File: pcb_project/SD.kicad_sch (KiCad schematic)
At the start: 0 parts

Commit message: Create MicroSD circuit
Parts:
- added C1: 0.1 µF, symbol Device:C
- added C2: 10µF, symbol Device:C
- added J1: MEM2052-00-195-00-A, Project_Footprints:MEM20520019500A, symbol MEM2052-00-195-00-A:MEM2052-00-195-00-A
- added R1, R2, R3, R4, R5, R6: 10k, symbol Device:R
- added R10, R11, R12, R7, R8, R9: R, symbol Device:R
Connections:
- new net: J1.7 (DAT0), R1.2, R7.2
- new net: J1.2 (CD/DAT3), R10.2, R4.2
- new net: J1.8 (DAT1), R2.2, R8.2
- new net: J1.3 (CMD), R11.2, R5.2
- new net: J1.1 (DAT2), R3.2, R9.2
- new net: J1.5 (CLK), R12.2
- new net +3V3: C1.1, C2.1, J1.4 (VDD), R1.1, R2.1, R3.1, R4.1, R5.1, R6.1
- new net GND: C1.2, C2.2, J1.6 (VSS), J1.G1 (GND_1), J1.G2 (GND_2), J1.G3 (GND_3), J1.G4 (GND_4)
- new net SDMMC_CLK: R12.1
- new net SDMMC_CMD: R11.1
- new net SDMMC_DAT0: R7.1
- new net SDMMC_DAT1: R8.1
- new net SDMMC_DAT2: R9.1
- new net SDMMC_DAT3: R10.1
- new net SD_CD: J1.9 (CD_PIN), R6.2
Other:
- note added: "R7-R12 should be physically close to MCU"

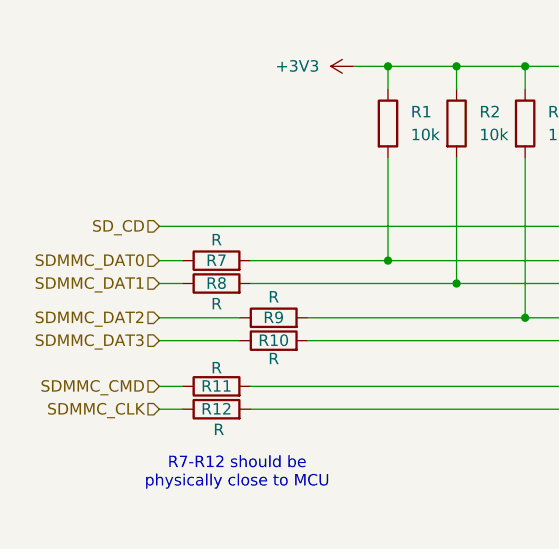
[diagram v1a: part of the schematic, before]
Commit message: Create power supply circuit
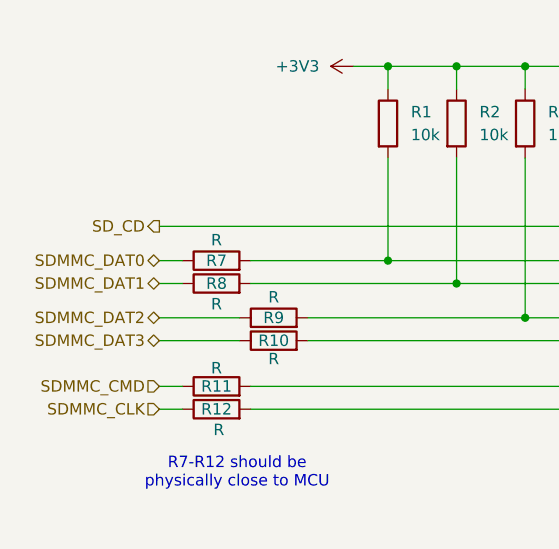
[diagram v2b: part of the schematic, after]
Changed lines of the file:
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@@
 	)
 	(hierarchical_label "SDMMC_DAT2"
-		(shape input)
+		(shape bidirectional)
 		(at 109.22 85.09 180)
 		(effects
@@
 	)
 	(hierarchical_label "SDMMC_DAT0"
-		(shape input)
+		(shape bidirectional)
 		(at 109.22 78.74 180)
 		(effects
@@
 	)
 	(hierarchical_label "SD_CD"
-		(shape input)
+		(shape output)
 		(at 109.22 74.93 180)
 		(effects
@@
 	)
 	(hierarchical_label "SDMMC_DAT3"
-		(shape input)
+		(shape bidirectional)
 		(at 109.22 87.63 180)
 		(effects
@@
 	)
 	(hierarchical_label "SDMMC_DAT1"
-		(shape input)
+		(shape bidirectional)
 		(at 109.22 81.28 180)
 		(effects

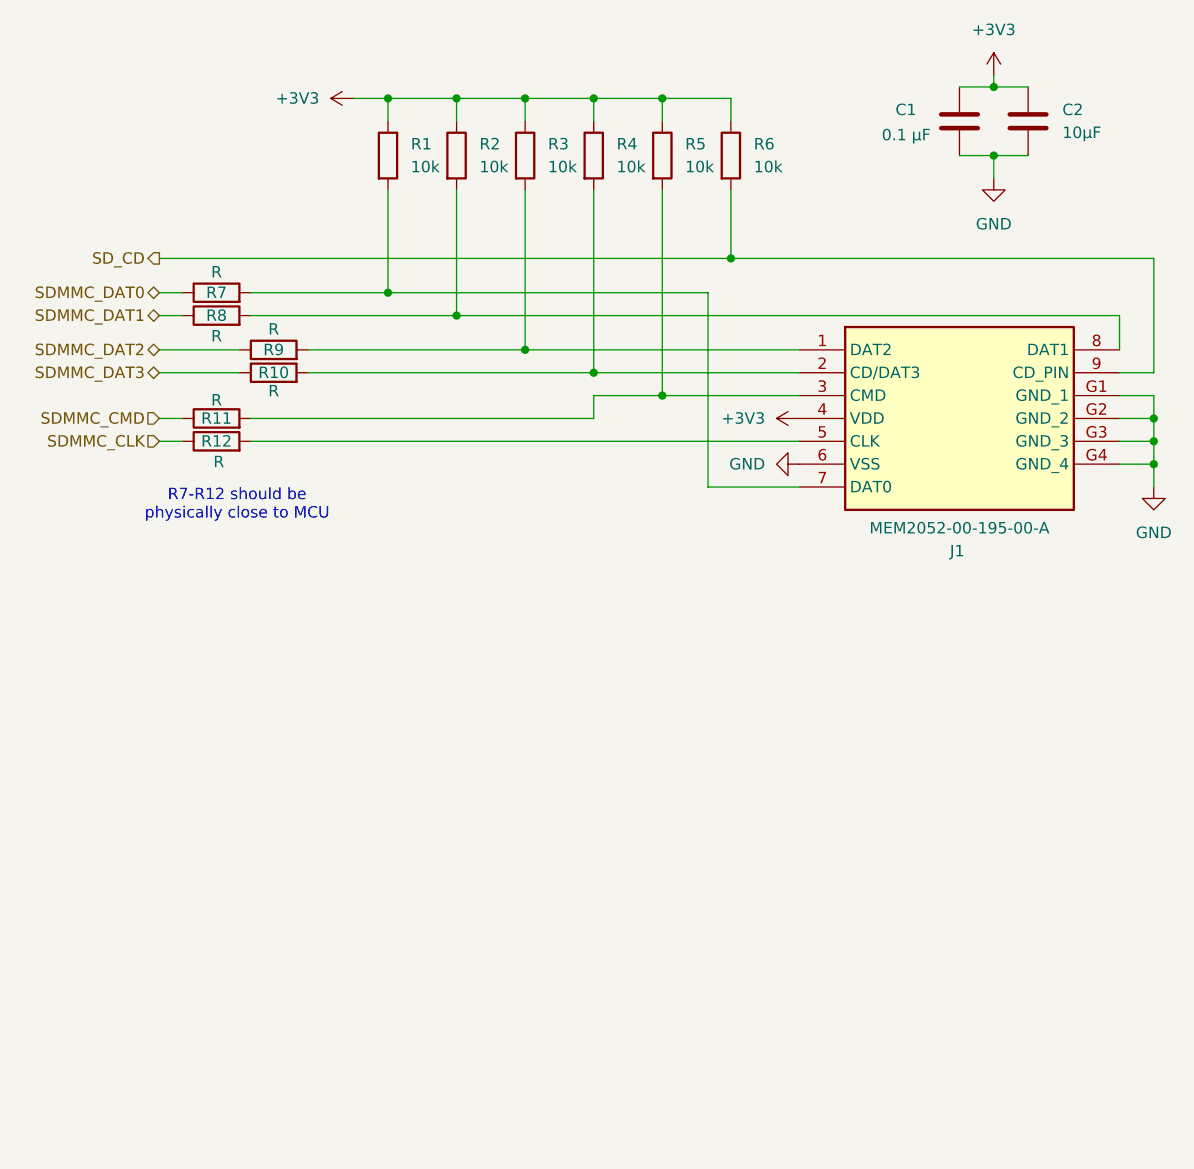
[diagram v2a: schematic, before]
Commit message: Add ESB protection to MicroSd reader
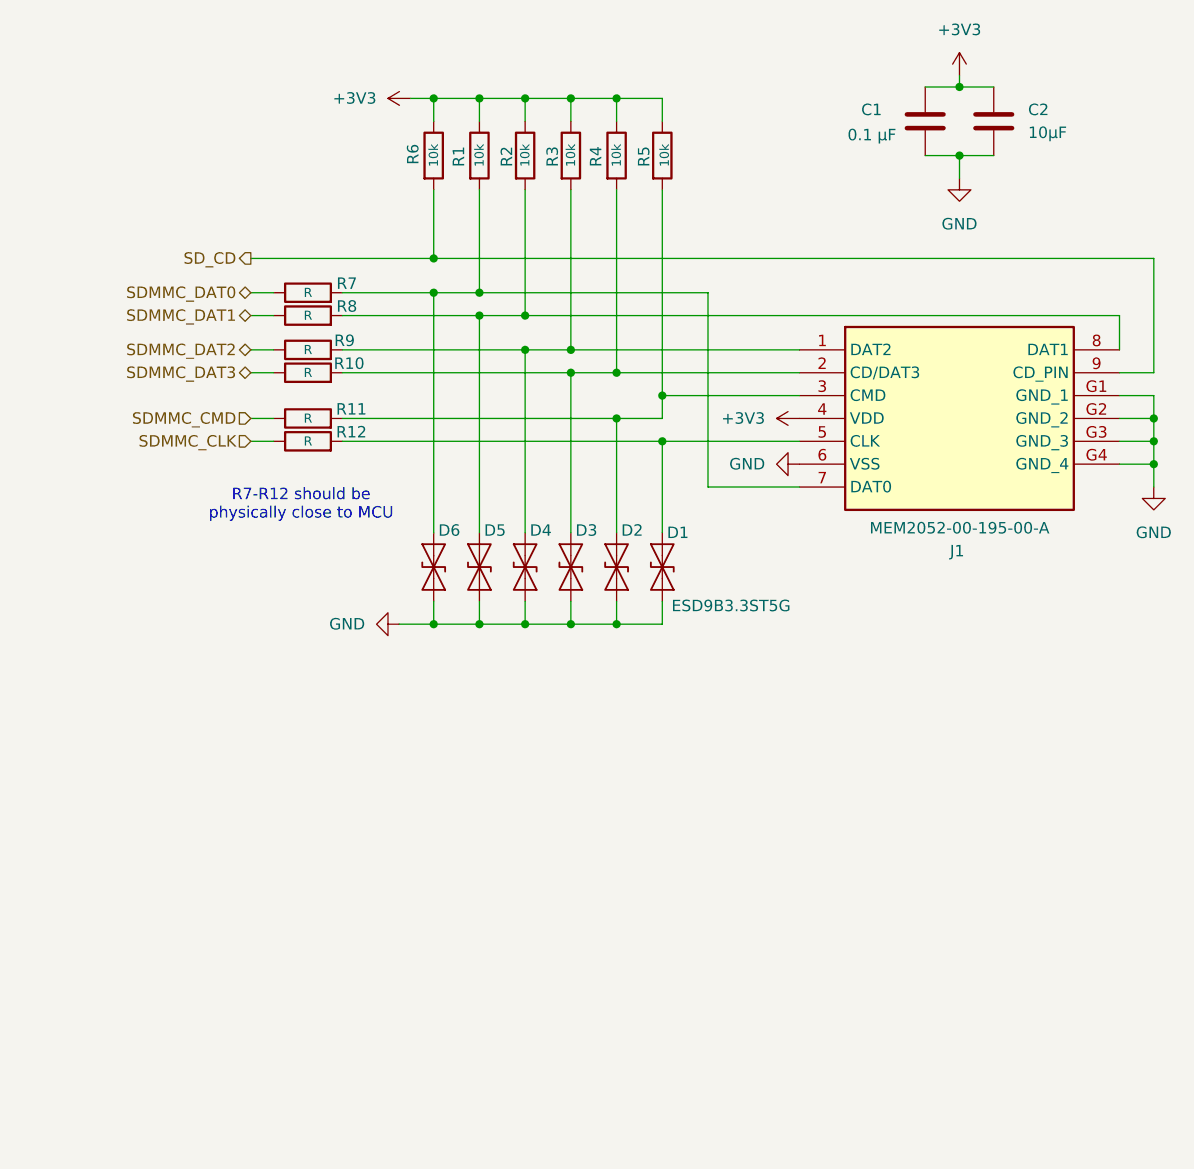
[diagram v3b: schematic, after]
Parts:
- added D1, D2, D3, D4, D5, D6: ESD9B3.3ST5G, Diode_SMD:D_SOD-923, symbol Diode:ESD9B3.3ST5G
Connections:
- net GND: now also D1.1 (A1), D2.2 (A2), D3.2 (A2), D4.2 (A2), D5.2 (A2), D6.2 (A2)
- net at J1.7 (DAT0), R1.2, R7.2: now also D6.1 (A1)
- net at J1.2 (CD/DAT3), R10.2, R4.2: now also D3.1 (A1)
- net at J1.8 (DAT1), R2.2, R8.2: now also D5.1 (A1)
- net at J1.3 (CMD), R11.2, R5.2: now also D2.1 (A1)
- net at J1.1 (DAT2), R3.2, R9.2: now also D4.1 (A1)
- net at J1.5 (CLK), R12.2: now also D1.2 (A2)
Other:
- moved on the sheet: C1, C2, R1, R10, R11, R12, R2, R3, R4, R6, R7, R8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

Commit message: ERC fixes, some remain
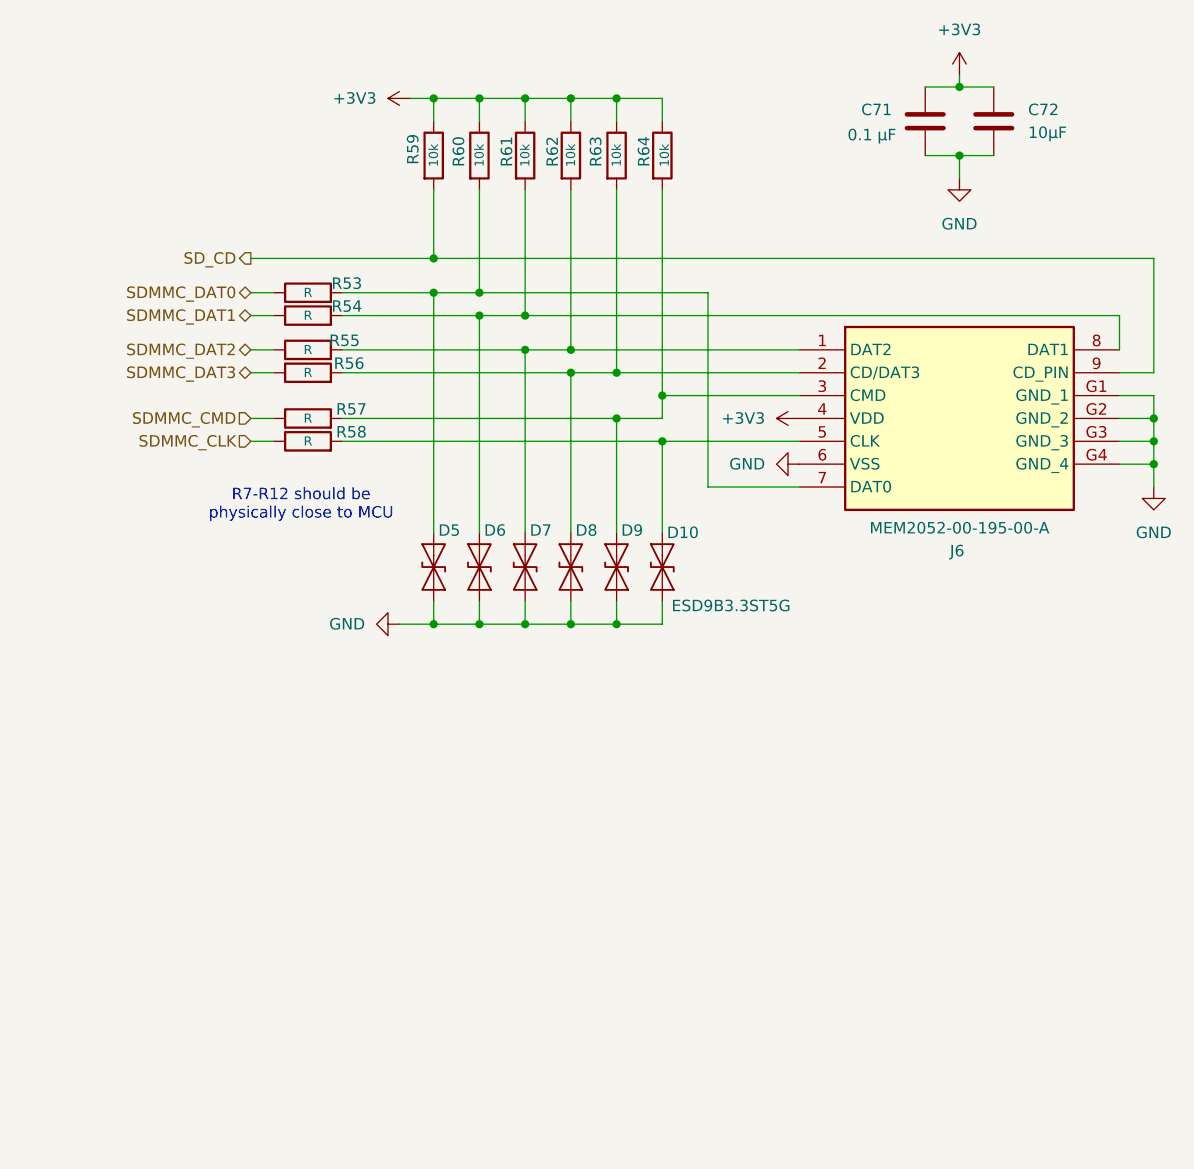
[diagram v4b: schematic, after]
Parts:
- renumbered C1 to C71, C2 to C72, D1 to D10, D6 to D5, D5 to D6, D4 to D7, D3 to D8, D2 to D9, J1 to J6, R7 to R53, R8 to R54, R9 to R55, R10 to R56, R11 to R57, R12 to R58, R6 to R59, R1 to R60, R2 to R61, R3 to R62, R4 to R63, R5 to R64
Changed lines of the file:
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@@
 		(dnp no)
 		(fields_autoplaced yes)
-		(property "Reference" "#PWR02"
+		(property "Reference" "#PWR073"
 			(at 140.97 57.15 0)
 			(effects
@@
 			(project ""
 				(path "/98f80f66-4595-4d0f-90ca-59b2db6f447b/dc6b7bff-d1d4-46df-9320-1308e1eae973"
-					(reference "#PWR02")
+					(reference "#PWR073")
 					(unit 1)
 				)
@@
 		(on_board yes)
 		(dnp no)
-		(property "Reference" "R1"
+		(property "Reference" "R60"
 			(at 142.494 64.77 90)
 			(effects
@@
 			(project ""
 				(path "/98f80f66-4595-4d0f-90ca-59b2db6f447b/dc6b7bff-d1d4-46df-9320-1308e1eae973"
-					(reference "R1")
+					(reference "R60")
 					(unit 1)
 				)
@@
 		(on_board yes)
 		(dnp no)
-		(property "Reference" "R4"
+		(property "Reference" "R63"
 			(at 157.734 64.77 90)
 			(effects
@@
 			(project "pcb_project"
 				(path "/98f80f66-4595-4d0f-90ca-59b2db6f447b/dc6b7bff-d1d4-46df-9320-1308e1eae973"
-					(reference "R4")
+					(reference "R63")
 					(unit 1)
 				)
@@
 		(dnp no)
 		(fields_autoplaced yes)
-		(property "Reference" "#PWR03"
+		(property "Reference" "#PWR075"
 			(at 173.99 97.79 0)
 			(effects
@@
 			(project ""
 				(path "/98f80f66-4595-4d0f-90ca-59b2db6f447b/dc6b7bff-d1d4-46df-9320-1308e1eae973"
-					(reference "#PWR03")
+					(reference "#PWR075")
 					(unit 1)
 				)
@@
 		(dnp no)
 		(fields_autoplaced yes)
-		(property "Reference" "#PWR04"
+		(property "Reference" "#PWR074"
 			(at 184.15 92.71 0)
 			(effects
@@
 			(project ""
 				(path "/98f80f66-4595-4d0f-90ca-59b2db6f447b/dc6b7bff-d1d4-46df-9320-1308e1eae973"
-					(reference "#PWR04")
+					(reference "#PWR074")
 					(unit 1)
 				)
@@
 		(on_board yes)
 		(dnp no)
-		(property "Reference" "D4"
+		(property "Reference" "D7"
 			(at 150.368 105.156 90)
 			(effects
@@
 			(project "pcb_project"
 				(path "/98f80f66-4595-4d0f-90ca-59b2db6f447b/dc6b7bff-d1d4-46df-9320-1308e1eae973"
-					(reference "D4")
+					(reference "D7")
 					(unit 1)
 				)
@@
 		(on_board yes)
 		(dnp no)
-		(property "Reference" "D2"
+		(property "Reference" "D9"
 			(at 160.528 105.156 90)
 			(effects
@@
 			(project "pcb_project"
 				(path "/98f80f66-4595-4d0f-90ca-59b2db6f447b/dc6b7bff-d1d4-46df-9320-1308e1eae973"
-					(reference "D2")
+					(reference "D9")
 					(unit 1)
 				)
@@
 		(on_board yes)
 		(dnp no)
-		(property "Reference" "R8"
+		(property "Reference" "R54"
 			(at 130.048 80.264 90)
 			(effects
@@
 			(project ""
 				(path "/98f80f66-4595-4d0f-90ca-59b2db6f447b/dc6b7bff-d1d4-46df-9320-1308e1eae973"
-					(reference "R8")
+					(reference "R54")
 					(unit 1)
 				)
@@
 		(on_board yes)
 		(dnp no)
-		(property "Reference" "R11"
+		(property "Reference" "R57"
 			(at 130.556 91.694 90)
 			(effects
@@
 			(project ""
 				(path "/98f80f66-4595-4d0f-90ca-59b2db6f447b/dc6b7bff-d1d4-46df-9320-1308e1eae973"
-					(reference "R11")
+					(reference "R57")
 					(unit 1)
 				)
@@
 		(on_board yes)
 		(dnp no)
-		(property "Reference" "D1"
+		(property "Reference" "D10"
 			(at 165.608 105.41 90)
 			(effects
@@
 			(project ""
 				(path "/98f80f66-4595-4d0f-90ca-59b2db6f447b/dc6b7bff-d1d4-46df-9320-1308e1eae973"
-					(reference "D1")
+					(reference "D10")
 					(unit 1)
 				)
@@
 		(dnp no)
 		(fields_autoplaced yes)
-		(property "Reference" "#PWR01"
+		(property "Reference" "#PWR078"
 			(at 219.71 106.68 0)
 			(effects
@@
 			(project ""
 				(path "/98f80f66-4595-4d0f-90ca-59b2db6f447b/dc6b7bff-d1d4-46df-9320-1308e1eae973"
-					(reference "#PWR01")
+					(reference "#PWR078")
 					(unit 1)
 				)
@@
 		(on_board yes)
 		(dnp no)
-		(property "Reference" "R7"
+		(property "Reference" "R53"
 			(at 130.048 77.724 90)
 			(effects
@@
 			(project ""
 				(path "/98f80f66-4595-4d0f-90ca-59b2db6f447b/dc6b7bff-d1d4-46df-9320-1308e1eae973"
-					(reference "R7")
+					(reference "R53")
 					(unit 1)
 				)
@@
 		(on_board yes)
 		(dnp no)
-		(property "Reference" "D5"
+		(property "Reference" "D6"
 			(at 145.288 105.156 90)
 			(effects
@@
 			(project "pcb_project"
 				(path "/98f80f66-4595-4d0f-90ca-59b2db6f447b/dc6b7bff-d1d4-46df-9320-1308e1eae973"
-					(reference "D5")
+					(reference "D6")
 					(unit 1)
 				)
@@
 		(on_board yes)
 		(dnp no)
-		(property "Reference" "R2"
+		(property "Reference" "R61"
 			(at 147.828 64.77 90)
 			(effects
@@
 			(project "pcb_project"
 				(path "/98f80f66-4595-4d0f-90ca-59b2db6f447b/dc6b7bff-d1d4-46df-9320-1308e1eae973"
-					(reference "R2")
+					(reference "R61")
 					(unit 1)
 				)
@@
 		(on_board yes)
 		(dnp no)
-		(property "Reference" "R5"
+		(property "Reference" "R64"
 			(at 163.068 64.77 90)
 			(effects
@@
 			(project "pcb_project"
 				(path "/98f80f66-4595-4d0f-90ca-59b2db6f447b/dc6b7bff-d1d4-46df-9320-1308e1eae973"
-					(reference "R5")
+					(reference "R64")
 					(unit 1)
 				)
@@
 		(dnp no)
 		(fields_autoplaced yes)
-		(property "Reference" "#PWR049"
+		(property "Reference" "#PWR072"
 			(at 129.54 115.57 0)
 			(effects
@@
 			(project ""
 				(path "/98f80f66-4595-4d0f-90ca-59b2db6f447b/dc6b7bff-d1d4-46df-9320-1308e1eae973"
-					(reference "#PWR049")
+					(reference "#PWR072")
 					(unit 1)
 				)
@@
 		(on_board yes)
 		(dnp no)
-		(property "Reference" "R9"
+		(property "Reference" "R55"
 			(at 129.794 84.074 90)
 			(effects
@@
 			(project ""
 				(path "/98f80f66-4595-4d0f-90ca-59b2db6f447b/dc6b7bff-d1d4-46df-9320-1308e1eae973"
-					(reference "R9")
+					(reference "R55")
 					(unit 1)
 				)
@@
 		(dnp no)
 		(fields_autoplaced yes)
-		(property "Reference" "#PWR06"
+		(property "Reference" "#PWR077"
 			(at 198.12 72.39 0)
 			(effects
@@
 			(project ""
 				(path "/98f80f66-4595-4d0f-90ca-59b2db6f447b/dc6b7bff-d1d4-46df-9320-1308e1eae973"
-					(reference "#PWR06")
+					(reference "#PWR077")
 					(unit 1)
 				)
@@
 		(on_board yes)
 		(dnp no)
-		(property "Reference" "R6"
+		(property "Reference" "R59"
 			(at 137.414 64.516 90)
 			(effects
@@
 			(project ""
 				(path "/98f80f66-4595-4d0f-90ca-59b2db6f447b/dc6b7bff-d1d4-46df-9320-1308e1eae973"
-					(reference "R6")
+					(reference "R59")
 					(unit 1)
 				)
@@
 		(on_board yes)
 		(dnp no)
-		(property "Reference" "D6"
+		(property "Reference" "D5"
 			(at 140.208 105.156 90)
 			(effects
@@
 			(project "pcb_project"
 				(path "/98f80f66-4595-4d0f-90ca-59b2db6f447b/dc6b7bff-d1d4-46df-9320-1308e1eae973"
-					(reference "D6")
+					(reference "D5")
 					(unit 1)
 				)
@@
 		(on_board yes)
 		(dnp no)
-		(property "Reference" "C1"
+		(property "Reference" "C71"
 			(at 187.198 58.42 0)
 			(effects
@@
 			(project ""
 				(path "/98f80f66-4595-4d0f-90ca-59b2db6f447b/dc6b7bff-d1d4-46df-9320-1308e1eae973"
-					(reference "C1")
+					(reference "C71")
 					(unit 1)
 				)
@@
 		(dnp no)
 		(fields_autoplaced yes)
-		(property "Reference" "C2"
+		(property "Reference" "C72"
 			(at 205.74 58.4199 0)
 			(effects
@@
 			(project "pcb_project"
 				(path "/98f80f66-4595-4d0f-90ca-59b2db6f447b/dc6b7bff-d1d4-46df-9320-1308e1eae973"
-					(reference "C2")
+					(reference "C72")
 					(unit 1)
 				)
@@
 		(on_board yes)
 		(dnp no)
-		(property "Reference" "R12"
+		(property "Reference" "R58"
 			(at 130.556 94.234 90)
 			(effects
@@
 			(project ""
 				(path "/98f80f66-4595-4d0f-90ca-59b2db6f447b/dc6b7bff-d1d4-46df-9320-1308e1eae973"
-					(reference "R12")
+					(reference "R58")
 					(unit 1)
 				)
@@
 		(on_board yes)
 		(dnp no)
-		(property "Reference" "R10"
+		(property "Reference" "R56"
 			(at 130.302 86.614 90)
 			(effects
@@
 			(project ""
 				(path "/98f80f66-4595-4d0f-90ca-59b2db6f447b/dc6b7bff-d1d4-46df-9320-1308e1eae973"
-					(reference "R10")
+					(reference "R56")
 					(unit 1)
 				)
@@
 		(on_board yes)
 		(dnp no)
-		(property "Reference" "#PWR05"
+		(property "Reference" "#PWR076"
 			(at 198.12 58.42 0)
 			(effects
@@
 			(project ""
 				(path "/98f80f66-4595-4d0f-90ca-59b2db6f447b/dc6b7bff-d1d4-46df-9320-1308e1eae973"
-					(reference "#PWR05")
+					(reference "#PWR076")
 					(unit 1)
 				)
@@
 		(on_board yes)
 		(dnp no)
-		(property "Reference" "J1"
+		(property "Reference" "J6"
 			(at 197.866 107.442 0)
 			(effects
@@
 			(project ""
 				(path "/98f80f66-4595-4d0f-90ca-59b2db6f447b/dc6b7bff-d1d4-46df-9320-1308e1eae973"
-					(reference "J1")
+					(reference "J6")
 					(unit 1)
 				)
@@
 		(on_board yes)
 		(dnp no)
-		(property "Reference" "R3"
+		(property "Reference" "R62"
 			(at 152.908 64.77 90)
 			(effects
@@
 			(project "pcb_project"
 				(path "/98f80f66-4595-4d0f-90ca-59b2db6f447b/dc6b7bff-d1d4-46df-9320-1308e1eae973"
-					(reference "R3")
+					(reference "R62")
 					(unit 1)
 				)
@@
 		(on_board yes)
 		(dnp no)
-		(property "Reference" "D3"
+		(property "Reference" "D8"
 			(at 155.448 105.156 90)
 			(effects
@@
 			(project "pcb_project"
 				(path "/98f80f66-4595-4d0f-90ca-59b2db6f447b/dc6b7bff-d1d4-46df-9320-1308e1eae973"
-					(reference "D3")
-					(unit 1)
-				)
+					(reference "D8")
+					(unit 1)
+				)
